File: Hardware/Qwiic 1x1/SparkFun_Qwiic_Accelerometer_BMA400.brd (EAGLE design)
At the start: 25.4 x 25.4 mm, 56 parts, among them J1 QWIIC_RIGHT_ANGLE, J2 QWIIC_RIGHT_ANGLE, U1 BMA400

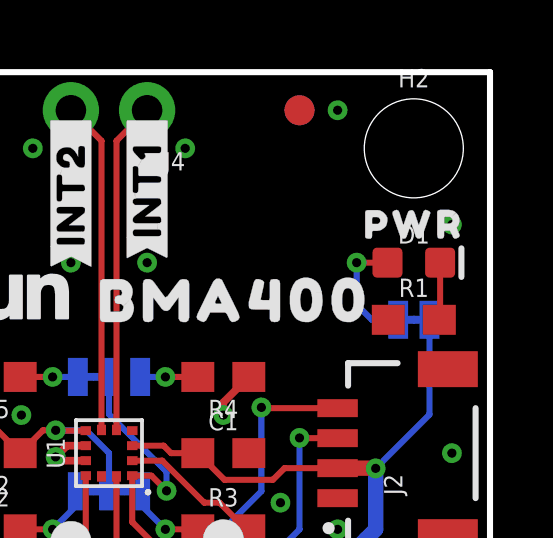
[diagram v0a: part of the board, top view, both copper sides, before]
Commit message: Design review updates
Add BMA400 voltage range to schematics
Add designer name to boards' tDocu
Add measures to 1x1
Adjust traces of micro
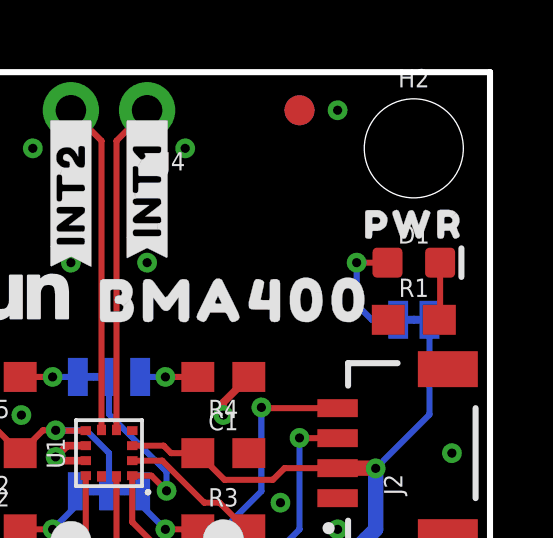
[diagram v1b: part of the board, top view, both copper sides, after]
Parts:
- moved FRAME1 8.03 mm to (-10.2, -29.2)
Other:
- board text added: "Dryw Wade"
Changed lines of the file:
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@@
 <drawing>
 <settings>
-<setting alwaysvectorfont="no"/>
+<setting alwaysvectorfont="yes"/>
 <setting verticaltext="up"/>
 </settings>
@@
 <text x="1.27" y="10.16" size="1.778" layer="16" font="vector" ratio="15" rot="MR270" align="center">v01</text>
 <rectangle x1="11.43" y1="13.716" x2="11.684" y2="14.351" layer="42"/>
+<text x="16.51" y="-29.21" size="1.778" layer="51" font="vector">Dryw Wade</text>
+<dimension x1="0" y1="0" x2="2.54" y2="0" x3="1.27" y3="-3.81" textsize="1.778" layer="47" unit="inch"/>
+<dimension x1="0" y1="0" x2="6.35" y2="0" x3="3.175" y3="-7.62" textsize="1.778" layer="47" unit="inch"/>
+<dimension x1="0" y1="0" x2="19.05" y2="0" x3="9.525" y3="-11.43" textsize="1.778" layer="47" unit="inch"/>
+<dimension x1="0" y1="0" x2="22.86" y2="0" x3="11.43" y3="-15.24" textsize="1.778" layer="47" unit="inch"/>
+<dimension x1="0" y1="0" x2="25.4" y2="0" x3="12.7" y3="-19.05" textsize="1.778" layer="47" unit="inch"/>
+<dimension x1="0" y1="0" x2="0" y2="2.54" x3="-1.27" y3="1.27" textsize="1.778" layer="47" unit="inch"/>
+<dimension x1="0" y1="0" x2="0" y2="22.86" x3="-5.08" y3="11.43" textsize="1.778" layer="47" unit="inch"/>
+<dimension x1="0" y1="0" x2="0" y2="25.4" x3="-8.89" y3="12.7" textsize="1.778" layer="47" unit="inch"/>
+<dimension x1="0" y1="25.4" x2="11.43" y2="25.4" x3="5.715" y3="26.67" textsize="1.778" layer="47" unit="inch"/>
+<dimension x1="0" y1="25.4" x2="13.97" y2="25.4" x3="6.985" y3="30.48" textsize="1.778" layer="47" unit="inch"/>
 </plain>
 <attributes>
@@
 </autorouter>
 <elements>
-<element name="FRAME1" library="SparkFun-Aesthetics" package="CREATIVE_COMMONS" value="FRAME-LETTER" x="-7.62" y="-21.59" smashed="yes">
-<attribute name="DESIGNER" value="" x="72.39" y="-22.86" size="1.778" layer="27" display="off"/>
-<attribute name="REV" value="" x="72.39" y="-22.86" size="1.778" layer="27" display="off"/>
+<element name="FRAME1" library="SparkFun-Aesthetics" package="CREATIVE_COMMONS" value="FRAME-LETTER" x="-10.16" y="-29.21" smashed="yes">
+<attribute name="DESIGNER" value="" x="69.85" y="-30.48" size="1.778" layer="27" display="off"/>
+<attribute name="REV" value="" x="69.85" y="-30.48" size="1.778" layer="27" display="off"/>
 </element>
 <element name="U1" library="BMA400" package="BMA400" value="BMA400" x="12.7" y="12.7" smashed="yes" rot="R90">
@@
 <via x="5.08" y="24.13" extent="1-16" drill="0.3048"/>
 <via x="20.32" y="24.13" extent="1-16" drill="0.3048"/>
-<via x="24.13" y="20.32" extent="1-16" drill="0.3048"/>
+<via x="24.003" y="20.447" extent="1-16" drill="0.3048"/>
 <via x="24.13" y="12.7" extent="1-16" drill="0.3048"/>
 <via x="1.27" y="12.7" extent="1-16" drill="0.3048"/>

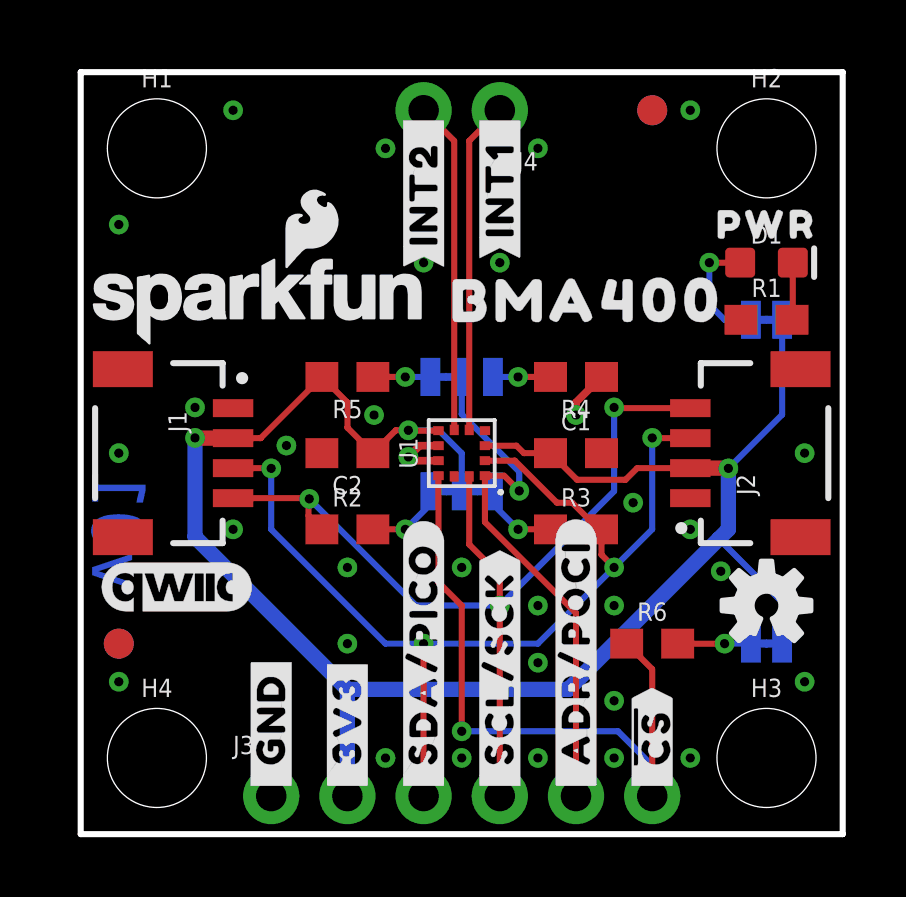
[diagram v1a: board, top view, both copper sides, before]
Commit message: Design review updates
Reduce silk labels on top side of 1x1
Adjust position of "BMA400" top silk of Micro
Rotate PWR jumper of Micro
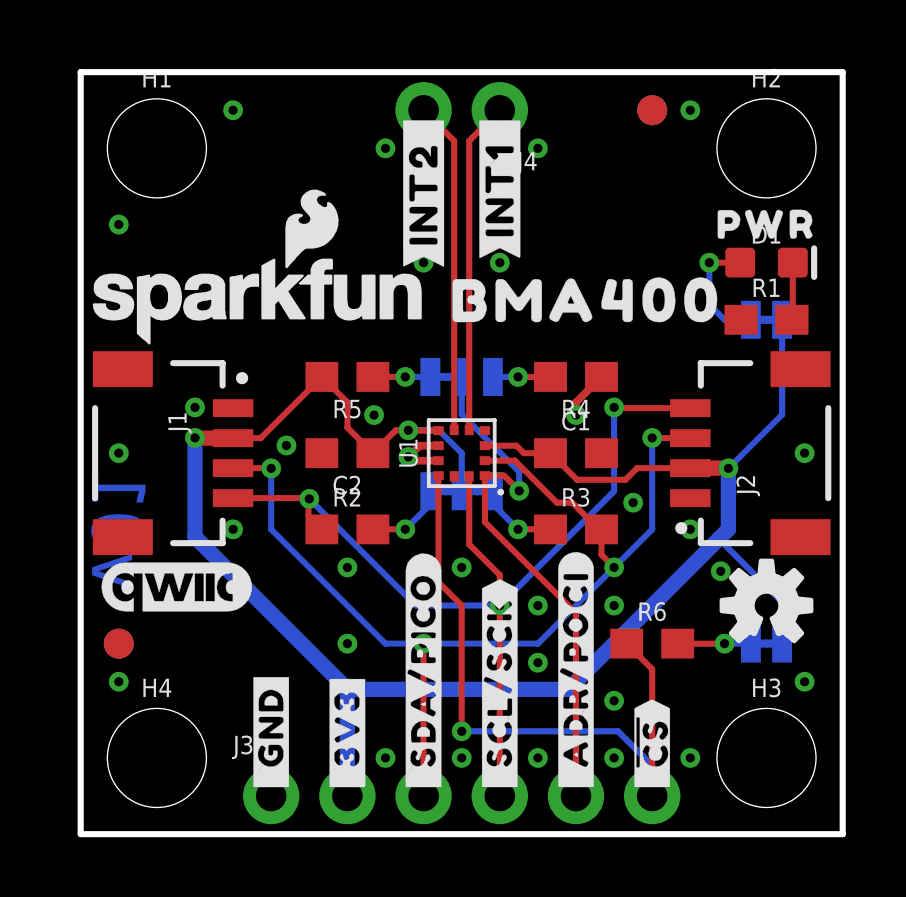
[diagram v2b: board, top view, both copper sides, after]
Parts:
- removed U$2: (no value), output:#_GND#0
- removed U$3: (no value), output:#_3V3#0
- added U$27: (no value), output:#_ADR#POCI#1
- added U$28: (no value), output:#_GND#6
- U$6: device output:#_SDA#PICO#0 -> output:#_3V3#6
- U$7: device output:#_SCL#SCK#0 -> output:#_SDA#PICO#5
- U$8: device output:#_ADR#POCI#0 -> output:#_#CS##2
- U$9: device output:#_#CS##0 -> output:#_SCL#SCK#3
- moved U$9 5.08 mm to (14.0, 1.27)
- moved U$7 2.54 mm to (11.4, 1.27)
- moved U$6 2.54 mm to (8.89, 1.27)
- moved U$8 2.54 mm to (19.1, 1.27)
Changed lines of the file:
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@@
 </element>
 <element name="U$1" library="output" package="PWR0" value="" x="22.86" y="20.32" smashed="yes"/>
-<element name="U$2" library="output" package="#_GND#0" value="" x="6.35" y="1.27" smashed="yes" rot="R90"/>
-<element name="U$3" library="output" package="#_3V3#0" value="" x="8.89" y="1.27" smashed="yes" rot="R90"/>
 <element name="U$4" library="output" package="#INT1_#0" value="" x="13.97" y="24.13" smashed="yes" rot="R90"/>
 <element name="U$5" library="output" package="#INT2_#0" value="" x="11.43" y="24.13" smashed="yes" rot="R90"/>
-<element name="U$6" library="output" package="#_SDA#PICO#0" value="" x="11.43" y="1.27" smashed="yes" rot="R90"/>
-<element name="U$7" library="output" package="#_SCL#SCK#0" value="" x="13.97" y="1.27" smashed="yes" rot="R90"/>
-<element name="U$8" library="output" package="#_ADR#POCI#0" value="" x="16.51" y="1.27" smashed="yes" rot="R90"/>
-<element name="U$9" library="output" package="#_#CS##0" value="" x="19.05" y="1.27" smashed="yes" rot="R90"/>
 <element name="U$10" library="output" package="#_GND#0" value="" x="6.35" y="1.27" smashed="yes" rot="MR90"/>
 <element name="U$11" library="output" package="#_3V3#0" value="" x="8.89" y="1.27" smashed="yes" rot="MR90"/>
@@
 <element name="U$25" library="output" package="##CS##0" value="" x="21.971" y="6.35" smashed="yes" rot="MR0"/>
 <element name="U$26" library="SparkFun-Aesthetics" package="SFE_LOGO_FLAME_.1" value="" x="3.81" y="6.35" smashed="yes" rot="MR0"/>
+<element name="U$27" library="output" package="#_ADR#POCI#1" value="" x="16.51" y="1.27" smashed="yes" rot="R90"/>
+<element name="U$8" library="output" package="#_#CS##2" value="" x="19.05" y="1.27" smashed="yes" rot="R90"/>
+<element name="U$9" library="output" package="#_SCL#SCK#3" value="" x="13.97" y="1.27" smashed="yes" rot="R90"/>
+<element name="U$7" library="output" package="#_SDA#PICO#5" value="" x="11.43" y="1.27" smashed="yes" rot="R90"/>
+<element name="U$6" library="output" package="#_3V3#6" value="" x="8.89" y="1.27" smashed="yes" rot="R90"/>
+<element name="U$28" library="output" package="#_GND#6" value="" x="6.35" y="1.27" smashed="yes" rot="R90"/>
 </elements>
 <signals>
